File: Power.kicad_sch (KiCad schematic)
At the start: 16 parts, among them J3 1986660-2, U4 AP63203WU

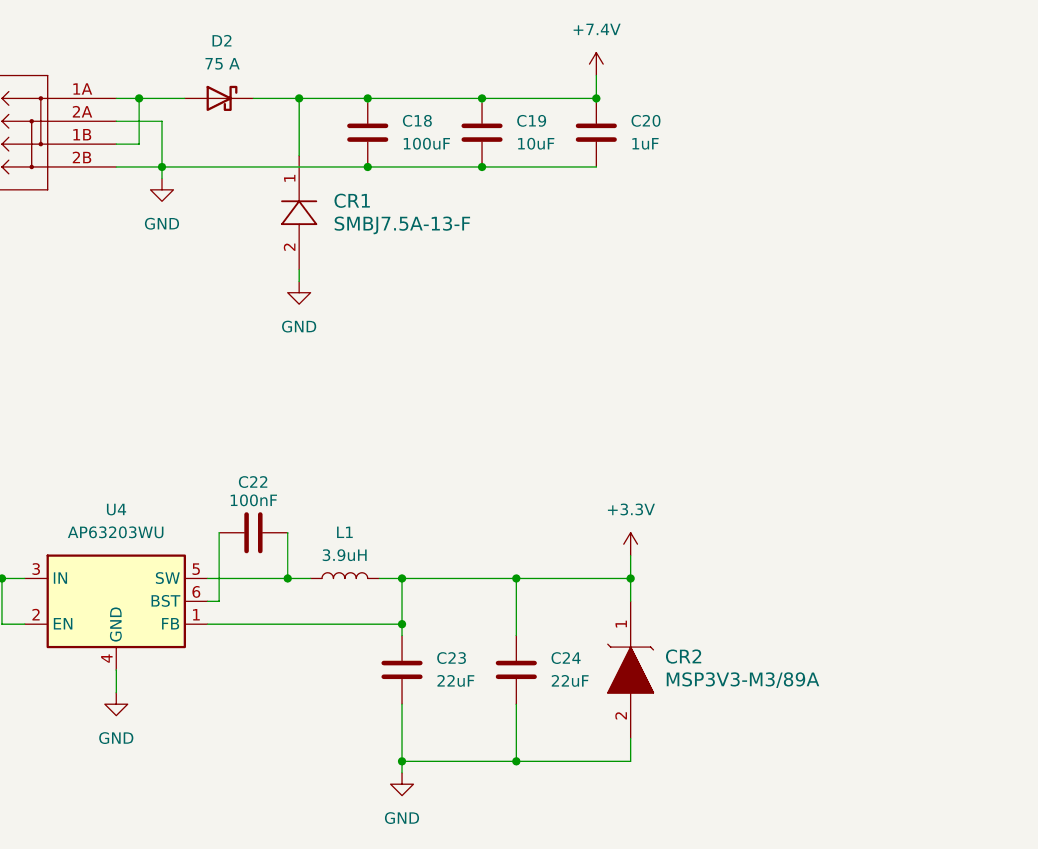
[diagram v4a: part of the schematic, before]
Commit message: Replace Schottky diode with P-channel mosfet circuit
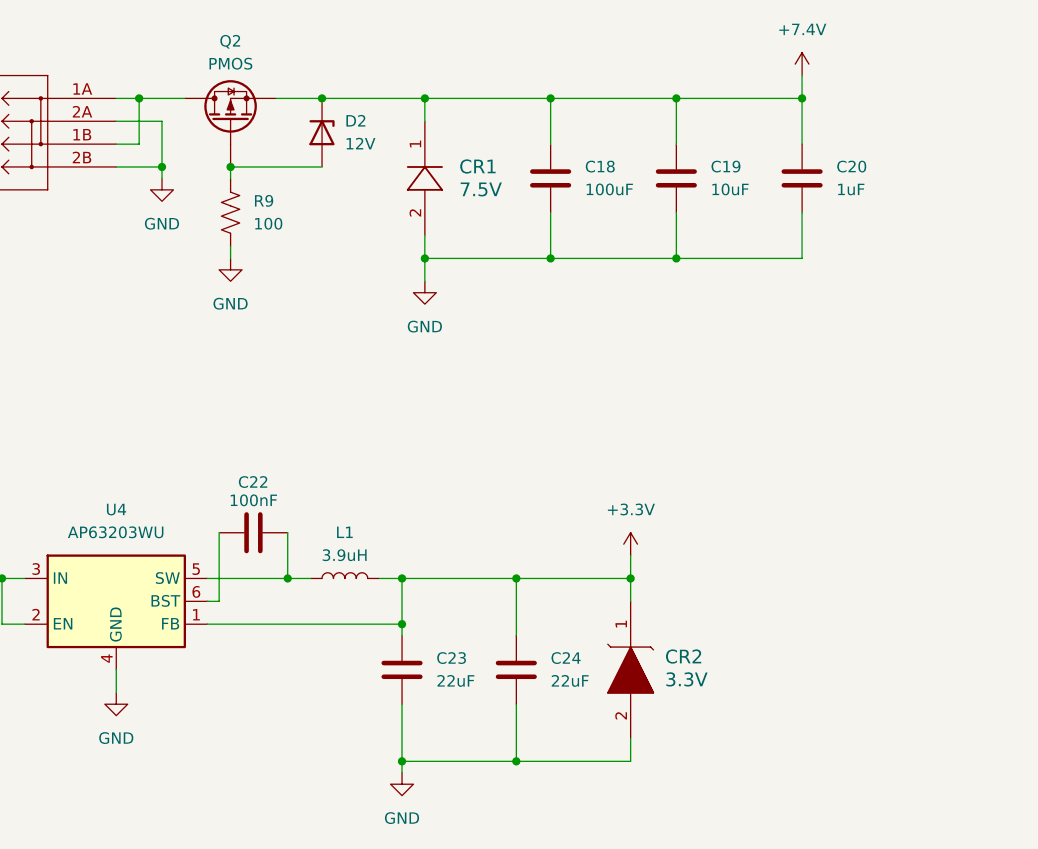
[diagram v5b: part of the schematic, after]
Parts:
- removed D2: 75 A, Package_TO_SOT_THT:TO-247-2_Vertical, symbol Device:D_Schottky
- added D2: 12V, Diode_SMD:D_SOD-123, symbol Device:D_Zener
- added Q2: PMOS, XuLab:SOP-Advance-8, symbol Device:Q_PMOS
- added R9: 100, Resistor_SMD:R_1206_3216Metric, symbol Device:R_US
- CR1: value SMBJ7.5A-13-F -> 7.5V
- CR2: value MSP3V3-M3/89A -> 3.3V
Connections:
- net +7.4V: now also D2.1 (K), Q2.1 (S)
- net GND: now also R9.2
- net at J3.1A, J3.1B: now also Q2.3 (D)
- new net: D2.2 (A), Q2.2 (G), R9.1
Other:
- moved on the sheet: C18, C19, C20, CR1

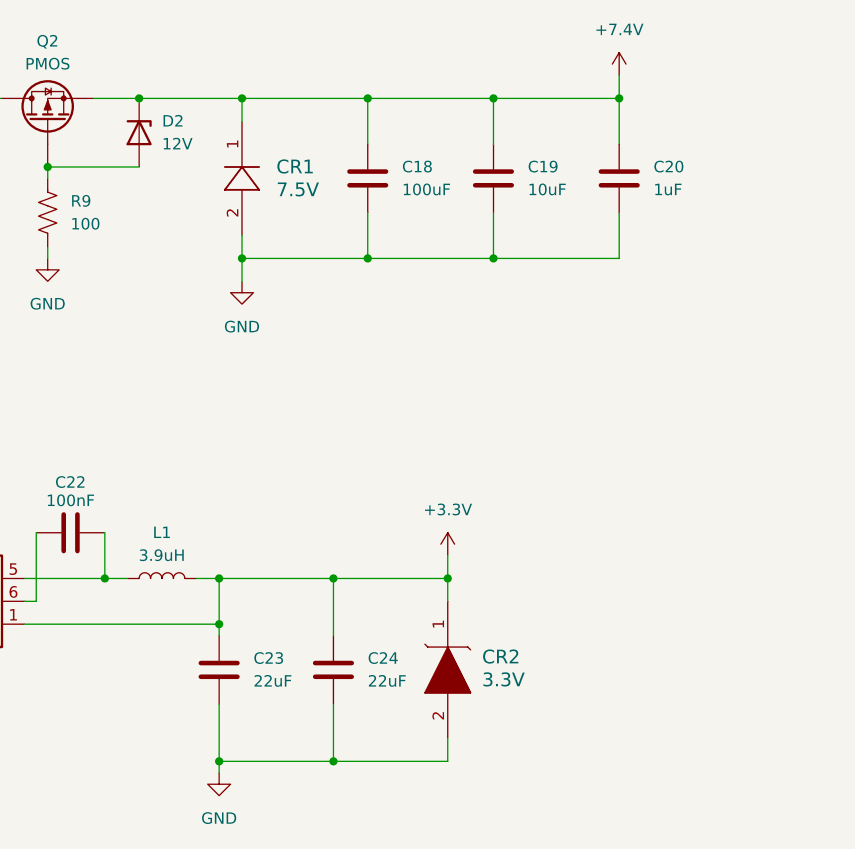
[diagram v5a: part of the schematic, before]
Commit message: Replace zener diode footprints with generics
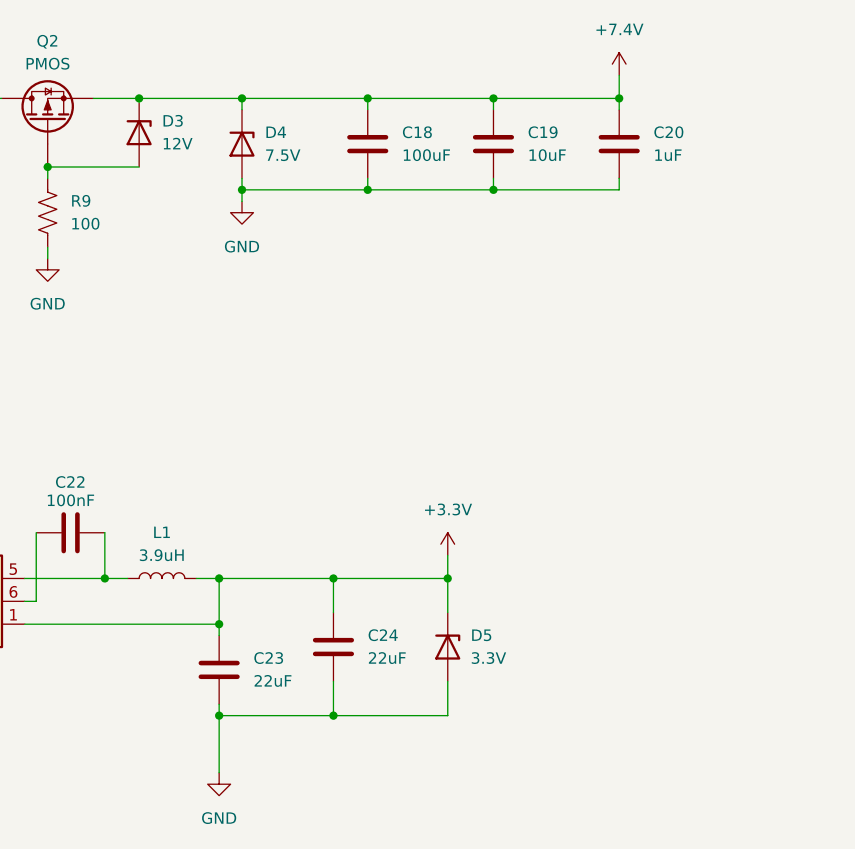
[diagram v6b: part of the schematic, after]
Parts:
- removed CR1: 7.5V, XuLab:SMB_DIO, symbol XuLab:SMBJ7.5A-13-F
- removed CR2: 3.3V, XuLab:DO-219AD_VIS, symbol XuLab:MSP3V3-M3_89A
- added D4: 7.5V, Diode_SMD:D_SMB, symbol Device:D_Zener
- added D5: 3.3V, Diode_SMD:D_MicroSMP_KA, symbol Device:D_Zener
- renumbered D2 to D3
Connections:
- net +3.3V: now also D5.1 (K)
- net +7.4V: now also D4.1 (K)
- net GND: now also D4.2 (A), D5.2 (A)
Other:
- moved on the sheet: C18, C19, C20, C24

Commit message: Add interchangeable field to BOM
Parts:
- C18, C19, C20, C21, C22, C23, C24, D3, D4, D5, R9: Interchangeable (none) -> Yes
- J3, L1, Q2, U4: Interchangeable (none) -> No
- TP1, TP2, TP3: Interchangeable (none) -> N/A
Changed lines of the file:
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@@
+			)
+		)
+		(property "Interchangeable" "Yes"
+			(at 132.08 45.72 0)
+			(effects
+				(font
+					(size 1.27 1.27)
+				)
+				(hide yes)
 			)
 		)
@@
 			)
 		)
+		(property "Interchangeable" "N/A"
+			(at 228.6 50.8 0)
+			(effects
+				(font
+					(size 1.27 1.27)
+				)
+				(hide yes)
+			)
+		)
 		(pin "1"
 		)
@@
 			)
 		)
+		(property "Interchangeable" "Yes"
+			(at 90.17 45.72 90)
+			(effects
+				(font
+					(size 1.27 1.27)
+				)
+				(hide yes)
+			)
+		)
 		(pin "1"
 		)
@@
 			)
 		)
+		(property "Interchangeable" "No"
+			(at 68.58 43.18 90)
+			(effects
+				(font
+					(size 1.27 1.27)
+				)
+				(hide yes)
+			)
+		)
 		(pin "3"
 		)
@@
 			)
 		)
+		(property "Interchangeable" "Yes"
+			(at 87.63 104.14 0)
+			(effects
+				(font
+					(size 1.27 1.27)
+				)
+				(hide yes)
+			)
+		)
 		(pin "1"
 		)
@@
 			)
 		)
+		(property "Interchangeable" "N/A"
+			(at 228.6 38.1 0)
+			(effects
+				(font
+					(size 1.27 1.27)
+				)
+				(hide yes)
+			)
+		)
 		(pin "1"
 		)
@@
 		)
 		(property "Listing" "https://www.digikey.com/en/products/detail/samsung-electro-mechanics/CL32A107MPVNNNE/3889022"
+			(at 104.14 45.72 0)
+			(effects
+				(font
+					(size 1.27 1.27)
+				)
+				(hide yes)
+			)
+		)
+		(property "Interchangeable" "Yes"
 			(at 104.14 45.72 0)
 			(effects
@@
 			)
 		)
+		(property "Interchangeable" "Yes"
+			(at 38.1 99.06 0)
+			(effects
+				(font
+					(size 1.27 1.27)
+				)
+				(hide yes)
+			)
+		)
 		(pin "1"
 		)
@@
 			)
 		)
+		(property "Interchangeable" "No"
+			(at 81.28 93.98 90)
+			(effects
+				(font
+					(size 1.27 1.27)
+				)
+				(hide yes)
+			)
+		)
 		(pin "2"
 		)
@@
 			)
 		)
+		(property "Interchangeable" "Yes"
+			(at 100.33 101.6 0)
+			(effects
+				(font
+					(size 1.27 1.27)
+				)
+				(hide yes)
+			)
+		)
 		(pin "1"
 		)
@@
 			)
 		)
+		(property "Interchangeable" "Yes"
+			(at 78.74 44.45 90)
+			(effects
+				(font
+					(size 1.27 1.27)
+				)
+				(hide yes)
+			)
+		)
 		(pin "2"
 		)
@@
 			)
 		)
+		(property "Interchangeable" "No"
+			(at 55.88 96.52 0)
+			(effects
+				(font
+					(size 1.27 1.27)
+				)
+				(hide yes)
+			)
+		)
 		(pin "3"
 		)
@@
 			)
 		)
+		(property "Interchangeable" "Yes"
+			(at 113.03 101.6 90)
+			(effects
+				(font
+					(size 1.27 1.27)
+				)
+				(hide yes)
+			)
+		)
 		(pin "1"
 		)
@@
 			)
 		)
+		(property "Interchangeable" "N/A"
+			(at 228.6 44.45 0)
+			(effects
+				(font
+					(size 1.27 1.27)
+				)
+				(hide yes)
+			)
+		)
 		(pin "1"
 		)
@@
 			)
 		)
+		(property "Interchangeable" "Yes"
+			(at 71.12 88.9 90)
+			(effects
+				(font
+					(size 1.27 1.27)
+				)
+				(hide yes)
+			)
+		)
 		(pin "1"
 		)
@@
 			)
 		)
+		(property "Interchangeable" "Yes"
+			(at 118.11 45.72 0)
+			(effects
+				(font
+					(size 1.27 1.27)
+				)
+				(hide yes)
+			)
+		)
 		(pin "1"
 		)
@@
 		)
 		(property "Listing" "https://www.digikey.com/en/products/detail/koa-speer-electronics-inc/RK73B2BTTD101J/10248278"
+			(at 68.58 53.34 0)
+			(effects
+				(font
+					(size 1.27 1.27)
+				)
+				(hide yes)
+			)
+		)
+		(property "Interchangeable" "Yes"
 			(at 68.58 53.34 0)
 			(effects
@@
 			(at 44.45 44.45 0)
 			(effects
+				(font
+					(size 1.27 1.27)
+				)
+				(hide yes)
+			)
+		)
+		(property "Interchangeable" "No"
+			(at 44.45 44.45 0)
+			(effects

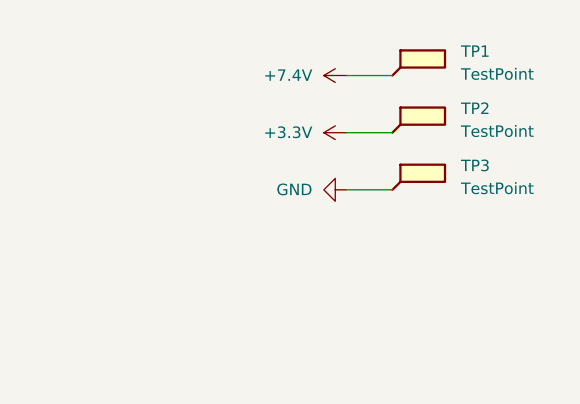
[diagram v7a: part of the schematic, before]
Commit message: Remove test points
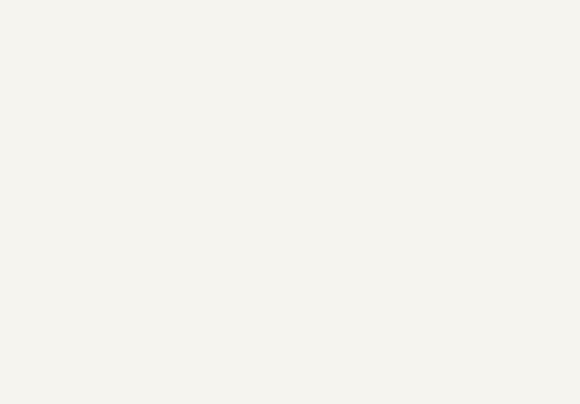
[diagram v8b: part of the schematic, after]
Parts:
- removed TP1, TP2, TP3: TestPoint, TestPoint:TestPoint_Plated_Hole_D2.0mm, symbol Connector:TestPoint_Flag
